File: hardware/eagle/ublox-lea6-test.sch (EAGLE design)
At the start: 52 parts, among them U1 UBLOX-LEA-6T, U2 TPS73633, U3 TPS73633, X1 SERIAL, X2 ANT, X3 FOUT, X4 ANT, X5 FOUT, X6 1PPS, X7 PC, X8 1PPS, X9 22-23-2021

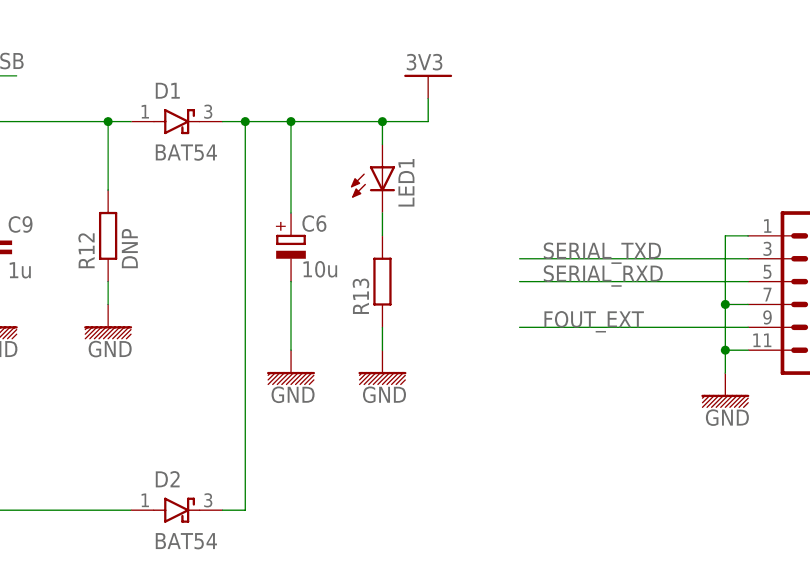
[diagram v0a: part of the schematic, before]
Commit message: Fixed up values and polygon signal
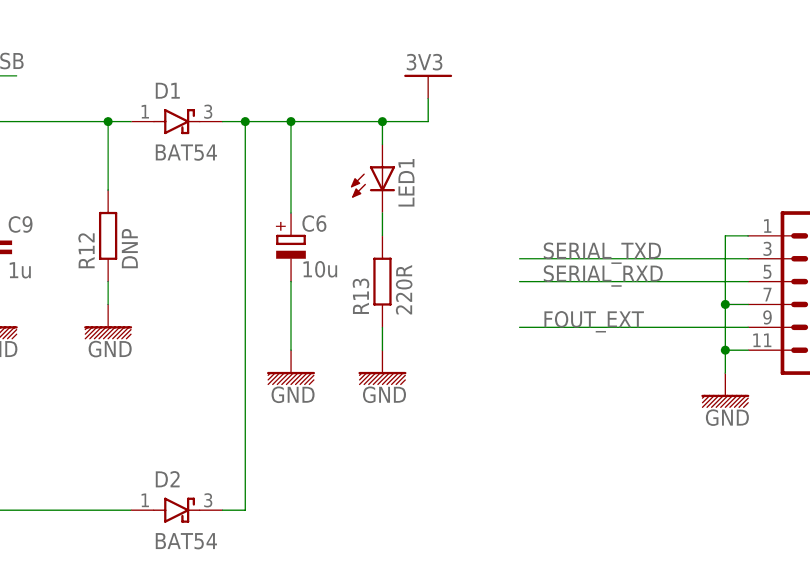
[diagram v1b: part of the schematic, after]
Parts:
- R13: value (none) -> 220R
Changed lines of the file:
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@@
 <?xml version="1.0" encoding="utf-8"?>
 <!DOCTYPE eagle SYSTEM "eagle.dtd">
-<eagle version="6.0">
+<eagle version="7.1.0">
 <drawing>
 <settings>
@@
 <part name="U$28" library="we_supply" deviceset="GND" device=""/>
 <part name="LED1" library="led" deviceset="LED" device="SML0603"/>
-<part name="R13" library="we_passive" deviceset="R-EU" device="_0603"/>
+<part name="R13" library="we_passive" deviceset="R-EU" device="_0603" value="220R"/>
 <part name="TP8" library="we_conn" deviceset="TESTPAD" device=""/>
 <part name="R14" library="we_passive" deviceset="R-EU" device="_0603" value="DNP"/>
